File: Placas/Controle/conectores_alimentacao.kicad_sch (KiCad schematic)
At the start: 11 parts, among them J1 Conn_02x02, J2 Conn_02x03, J3 Conn_02x02

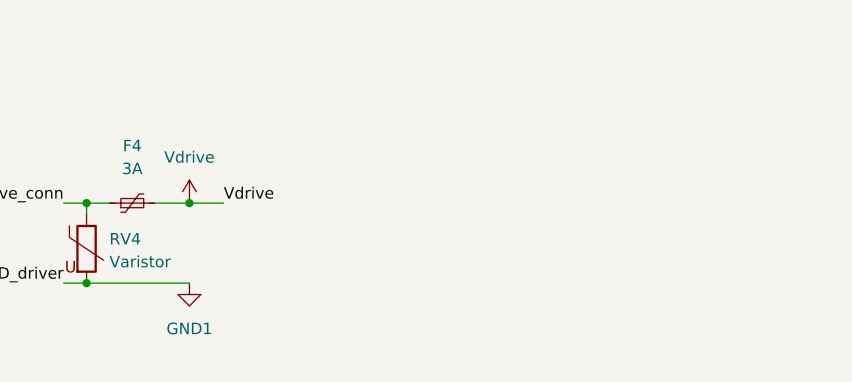
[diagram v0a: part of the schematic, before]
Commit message: Adição de circuitos opcionais para PWM
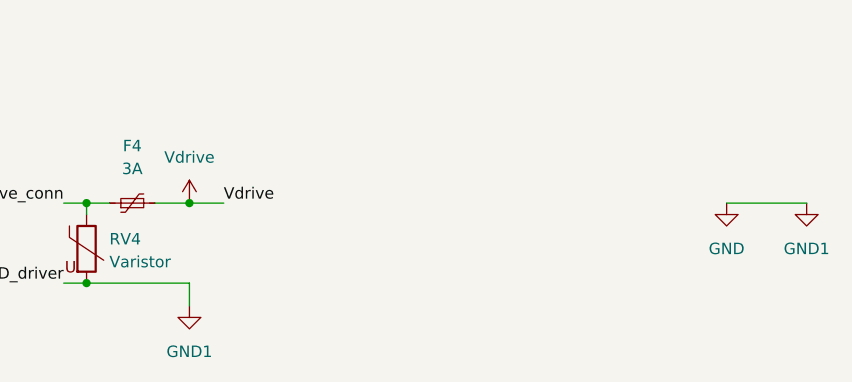
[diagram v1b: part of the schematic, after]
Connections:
- net GND1 is gone; now on net GND: J3.2 (Pin_2), J3.4 (Pin_4), RV4.2
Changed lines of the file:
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@@
+	(wire
+		(pts
+			(xy 92.71 125.73) (xy 92.71 128.27)
+		)
+		(stroke
+			(width 0)
+			(type default)
+		)
+	)
 	(wire
 		(pts
@@
 		(pts
 			(xy 81.28 26.67) (xy 83.82 26.67)
+		)
+		(stroke
+			(width 0)
+			(type default)
+		)
+	)
+	(wire
+		(pts
+			(xy 152.4 116.84) (xy 161.29 116.84)
 		)
 		(stroke
@@
 	)
 	(symbol
-		(lib_id "power:GND1")
-		(at 92.71 125.73 0)
-		(unit 1)
-		(exclude_from_sim no)
-		(in_bom yes)
-		(on_board yes)
-		(dnp no)
-		(fields_autoplaced yes)
-		(property "Reference" "#PWR6"
-			(at 92.71 132.08 0)
-			(effects
-				(font
-					(size 1.27 1.27)
-				)
-				(hide yes)
-			)
-		)
-		(property "Value" "GND1"
-			(at 92.71 130.81 0)
-			(effects
-				(font
-					(size 1.27 1.27)
-				)
-			)
-		)
-		(property "Footprint" ""
-			(at 92.71 125.73 0)
-			(effects
-				(font
-					(size 1.27 1.27)
-				)
-				(hide yes)
-			)
-		)
-		(property "Datasheet" ""
-			(at 92.71 125.73 0)
-			(effects
-				(font
-					(size 1.27 1.27)
-				)
-				(hide yes)
-			)
-		)
-		(property "Description" "Power symbol creates a global label with name \"GND1\" , ground"
-			(at 92.71 125.73 0)
-			(effects
-				(font
-					(size 1.27 1.27)
-				)
-				(hide yes)
-			)
-		)
-		(pin "1"
-		)
-		(instances
-			(project "board"
-				(path "/01568b53-f202-4f02-9c1a-9c10c7610b4b/82d14b7f-e7c0-46b8-aff5-dc2713e8f15c"
-					(reference "#PWR6")
-					(unit 1)
-				)
-			)
-			(project "board"
-				(path "/d7be55ed-3561-4de6-aa99-76e883d44fb9/f4133426-dc98-451a-9296-d9cf07231099"
-					(reference "#PWR41")
-					(unit 1)
-				)
-			)
-		)
-	)
-	(symbol
 		(lib_id "Device:Varistor")
 		(at 81.28 30.48 0)
@@
 	)
 	(symbol
+		(lib_id "power:GND1")
+		(at 92.71 128.27 0)
+		(unit 1)
+		(exclude_from_sim no)
+		(in_bom yes)
+		(on_board yes)
+		(dnp no)
+		(fields_autoplaced yes)
+		(property "Reference" "#PWR6"
+			(at 92.71 134.62 0)
+			(effects
+				(font
+					(size 1.27 1.27)
+				)
+				(hide yes)
+			)
+		)
+		(property "Value" "GND1"
+			(at 92.71 133.35 0)
+			(effects
+				(font
+					(size 1.27 1.27)
+				)
+			)
+		)
+		(property "Footprint" ""
+			(at 92.71 128.27 0)
+			(effects
+				(font
+					(size 1.27 1.27)
+				)
+				(hide yes)
+			)
+		)
+		(property "Datasheet" ""
+			(at 92.71 128.27 0)
+			(effects
+				(font
+					(size 1.27 1.27)
+				)
+				(hide yes)
+			)
+		)
+		(property "Description" "Power symbol creates a global label with name \"GND1\" , ground"
+			(at 92.71 128.27 0)
+			(effects
+				(font
+					(size 1.27 1.27)
+				)
+				(hide yes)
+			)
+		)
+		(pin "1"
+		)
+		(instances
+			(project ""
+				(path "/01568b53-f202-4f02-9c1a-9c10c7610b4b/82d14b7f-e7c0-46b8-aff5-dc2713e8f15c"
+					(reference "#PWR6")
+					(unit 1)
+				)
+			)
+		)
+	)
+	(symbol
 		(lib_id "Device:Varistor")
 		(at 81.28 66.04 0)
@@
 	)
 	(symbol
+		(lib_id "power:GND")
+		(at 152.4 116.84 0)
+		(unit 1)
+		(exclude_from_sim no)
+		(in_bom yes)
+		(on_board yes)
+		(dnp no)
+		(fields_autoplaced yes)
+		(property "Reference" "#PWR8"
+			(at 152.4 123.19 0)
+			(effects
+				(font
+					(size 1.27 1.27)
+				)
+				(hide yes)
+			)
+		)
+		(property "Value" "GND"
+			(at 152.4 121.92 0)
+			(effects
+				(font
+					(size 1.27 1.27)
+				)
+			)
+		)
+		(property "Footprint" ""
+			(at 152.4 116.84 0)
+			(effects
+				(font
+					(size 1.27 1.27)
+				)
+				(hide yes)
+			)
+		)
+		(property "Datasheet" ""
+			(at 152.4 116.84 0)
+			(effects
+				(font
+					(size 1.27 1.27)
+				)
+				(hide yes)
+			)
+		)
+		(property "Description" "Power symbol creates a global label with name \"GND\" , ground"
+			(at 152.4 116.84 0)
+			(effects
+				(font
+					(size 1.27 1.27)
+				)
+				(hide yes)
+			)
+		)
+		(pin "1"
+		)
+		(instances
+			(project "Controle"
+				(path "/01568b53-f202-4f02-9c1a-9c10c7610b4b/82d14b7f-e7c0-46b8-aff5-dc2713e8f15c"
+					(reference "#PWR8")
+					(unit 1)
+				)
+			)
+		)
+	)
+	(symbol
 		(lib_id "power:Vdrive")
 		(at 92.71 116.84 0)
@@
 					(unit 1)
 				)
+			)
+		)
+	)
+	(symbol
+		(lib_id "power:GND1")
+		(at 161.29 116.84 0)
+		(unit 1)
+		(exclude_from_sim no)
+		(in_bom yes)
+		(on_board yes)
+		(dnp no)
+		(fields_autoplaced yes)
+		(property "Reference" "#PWR9"
+			(at 161.29 123.19 0)
+			(effects
+				(font
+					(size 1.27 1.27)
+				)
+				(hide yes)
+			)
+		)
+		(property "Value" "GND1"
+			(at 161.29 121.92 0)
+			(effects
+				(font
+					(size 1.27 1.27)
+				)
+			)
+		)
+		(property "Footprint" ""
+			(at 161.29 116.84 0)
+			(effects
+				(font
+					(size 1.27 1.27)
+				)
+				(hide yes)
+			)
+		)
+		(property "Datasheet" ""
+			(at 161.29 116.84 0)
+			(effects
+				(font
+					(size 1.27 1.27)
+				)
+				(hide yes)
+			)
+		)
+		(property "Description" "Power symbol creates a global label with name \"GND1\" , ground"
+			(at 161.29 116.84 0)
+			(effects
+				(font
+					(size 1.27 1.27)
+				)
+				(hide yes)
+			)
+		)
+		(pin "1"
+		)
+		(instances
+			(project "Controle"
+				(path "/01568b53-f202-4f02-9c1a-9c10c7610b4b/82d14b7f-e7c0-46b8-aff5-dc2713e8f15c"
+					(reference "#PWR9")
+					(unit 1)
+				)

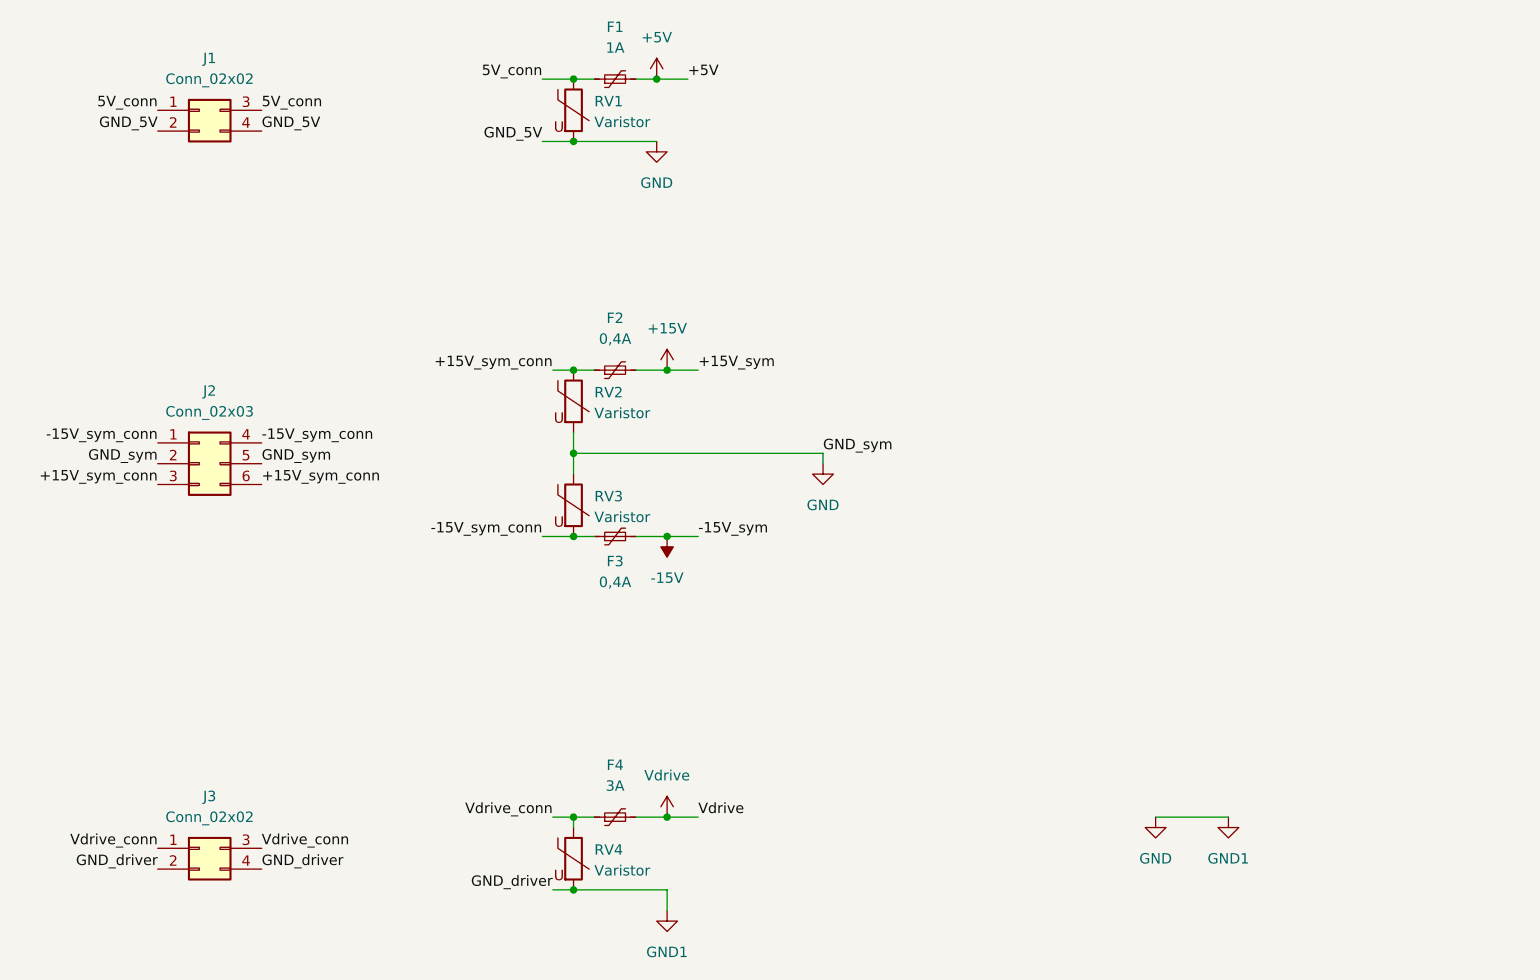
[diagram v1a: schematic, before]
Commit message: Modificações nas duas placas, adição de furos para montagem, melhora na posição dos micros e conectores para comunicação SPI
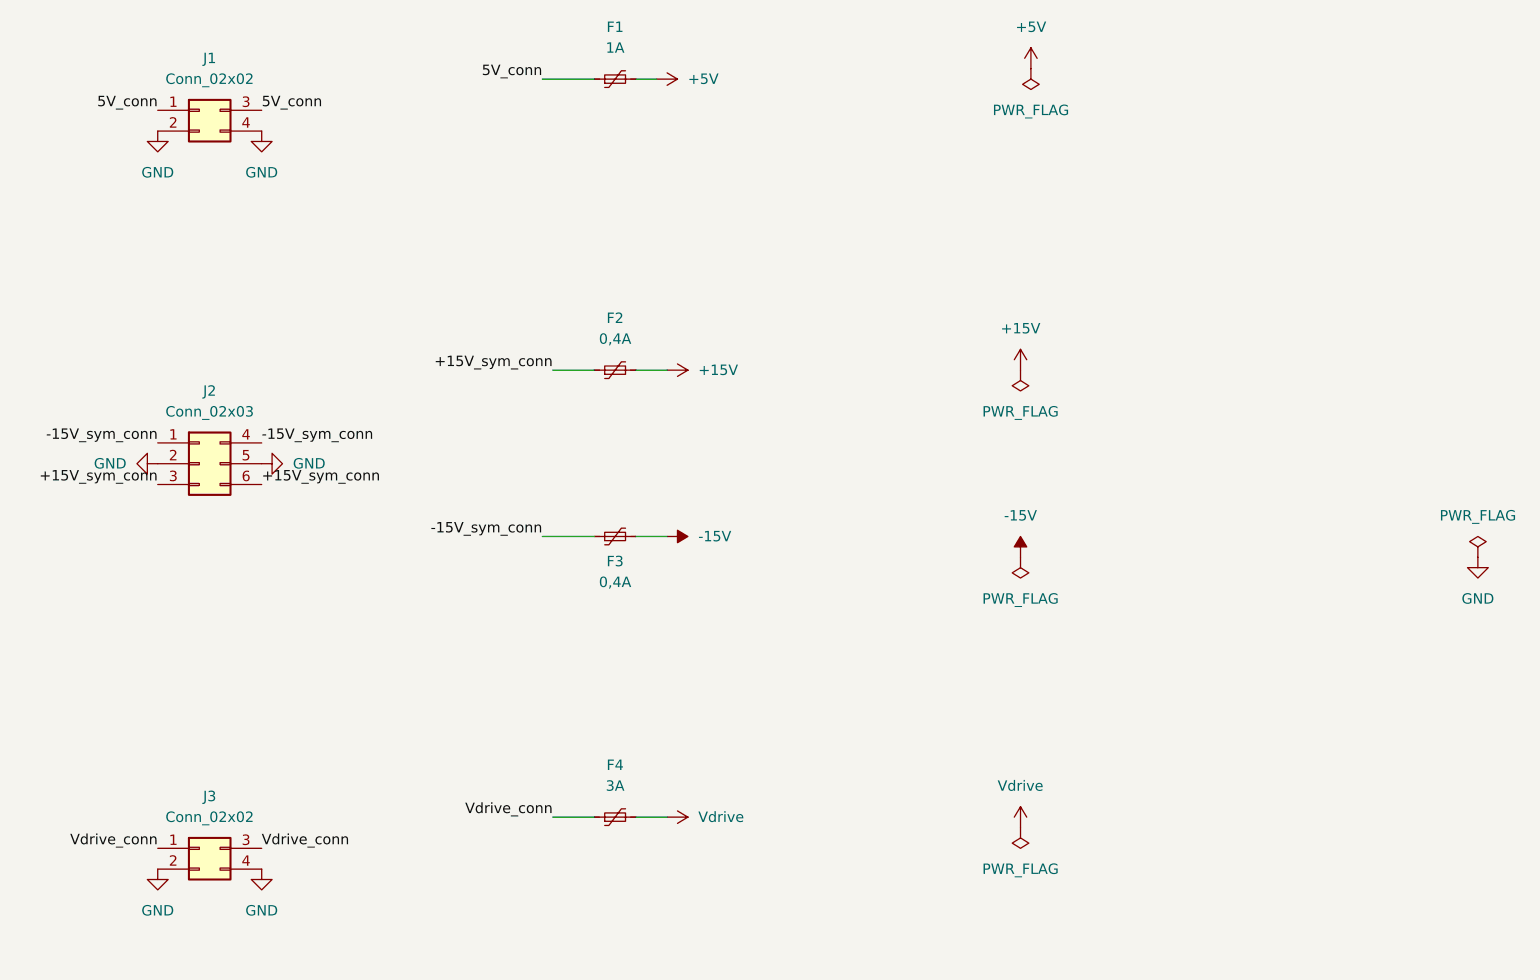
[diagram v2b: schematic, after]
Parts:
- removed RV1, RV2, RV3, RV4: Varistor, Varistor:RV_Disc_D12mm_W3.9mm_P7.5mm, symbol Device:Varistor
- F1, F2, F3, F4: footprint Fuse:Fuse_BelFuse_0ZRE0005FF_L8.3mm_W3.8mm -> Fuse:Fuse_1210_3225Metric_Pad1.42x2.65mm_HandSolder
